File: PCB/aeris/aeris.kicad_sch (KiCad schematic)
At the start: 28 parts, among them J1 SHT45, J2 LPS22HB, J3 SCD40, J4 SGP41, J5 PMSA003A, Q1 BSS138, U1 74AHCT244, U3 ESP32-H2-SUPERMINI

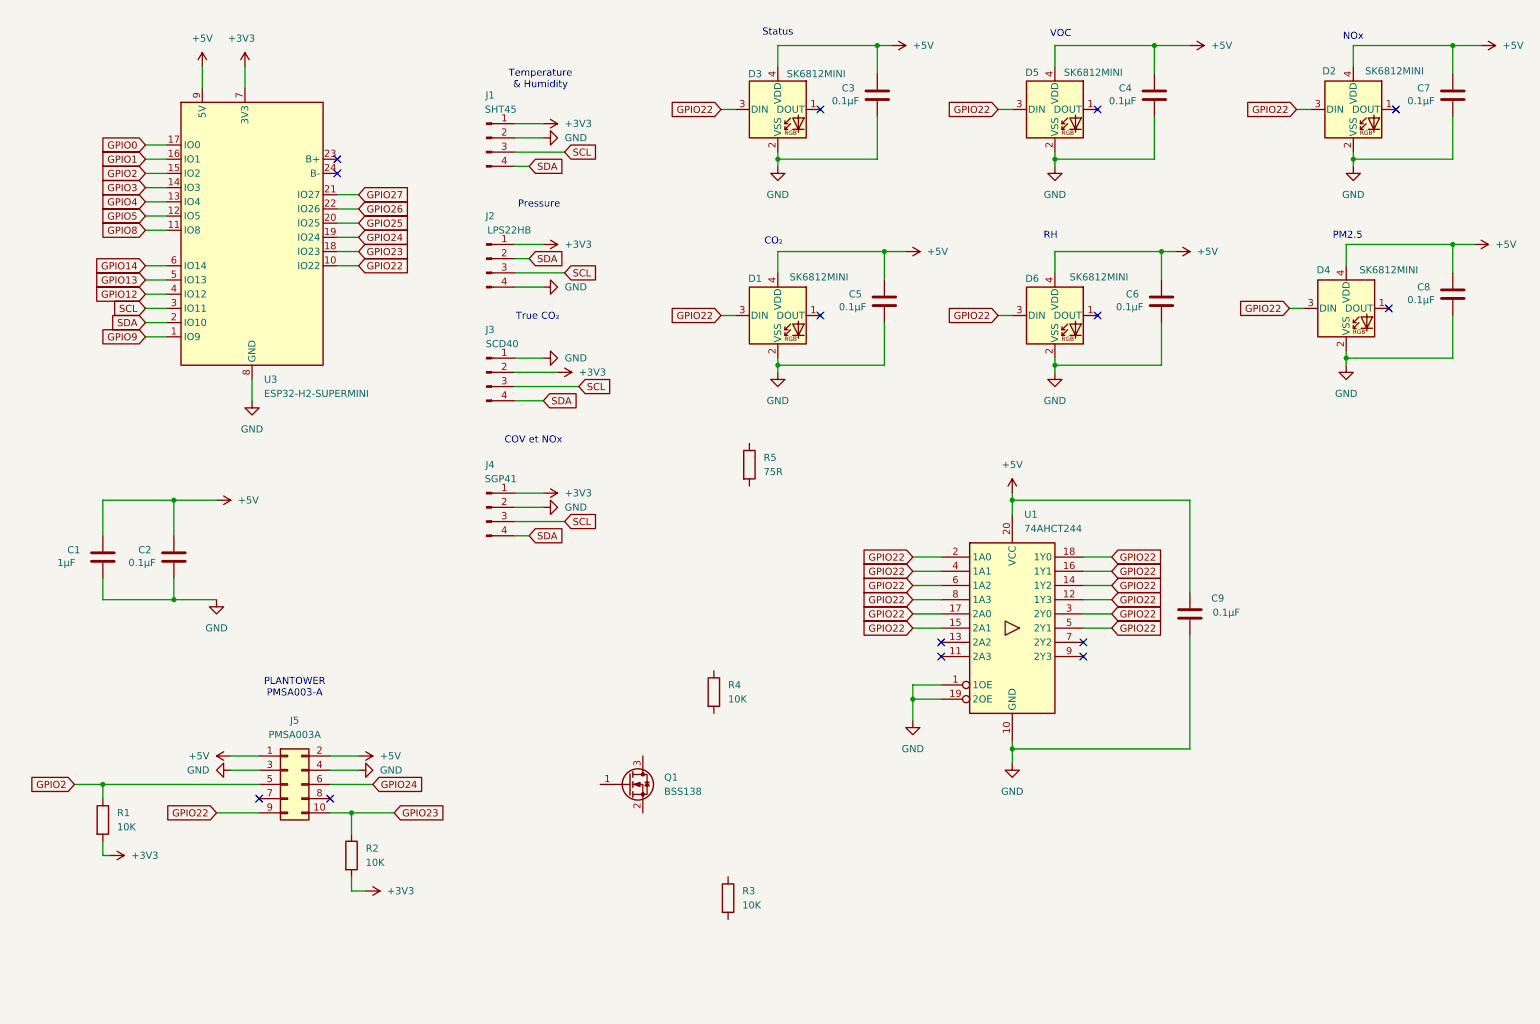
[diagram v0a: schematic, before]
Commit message: Add symbol library for ESP32-C6FH4-SuperMini to the project and update project GPIOs
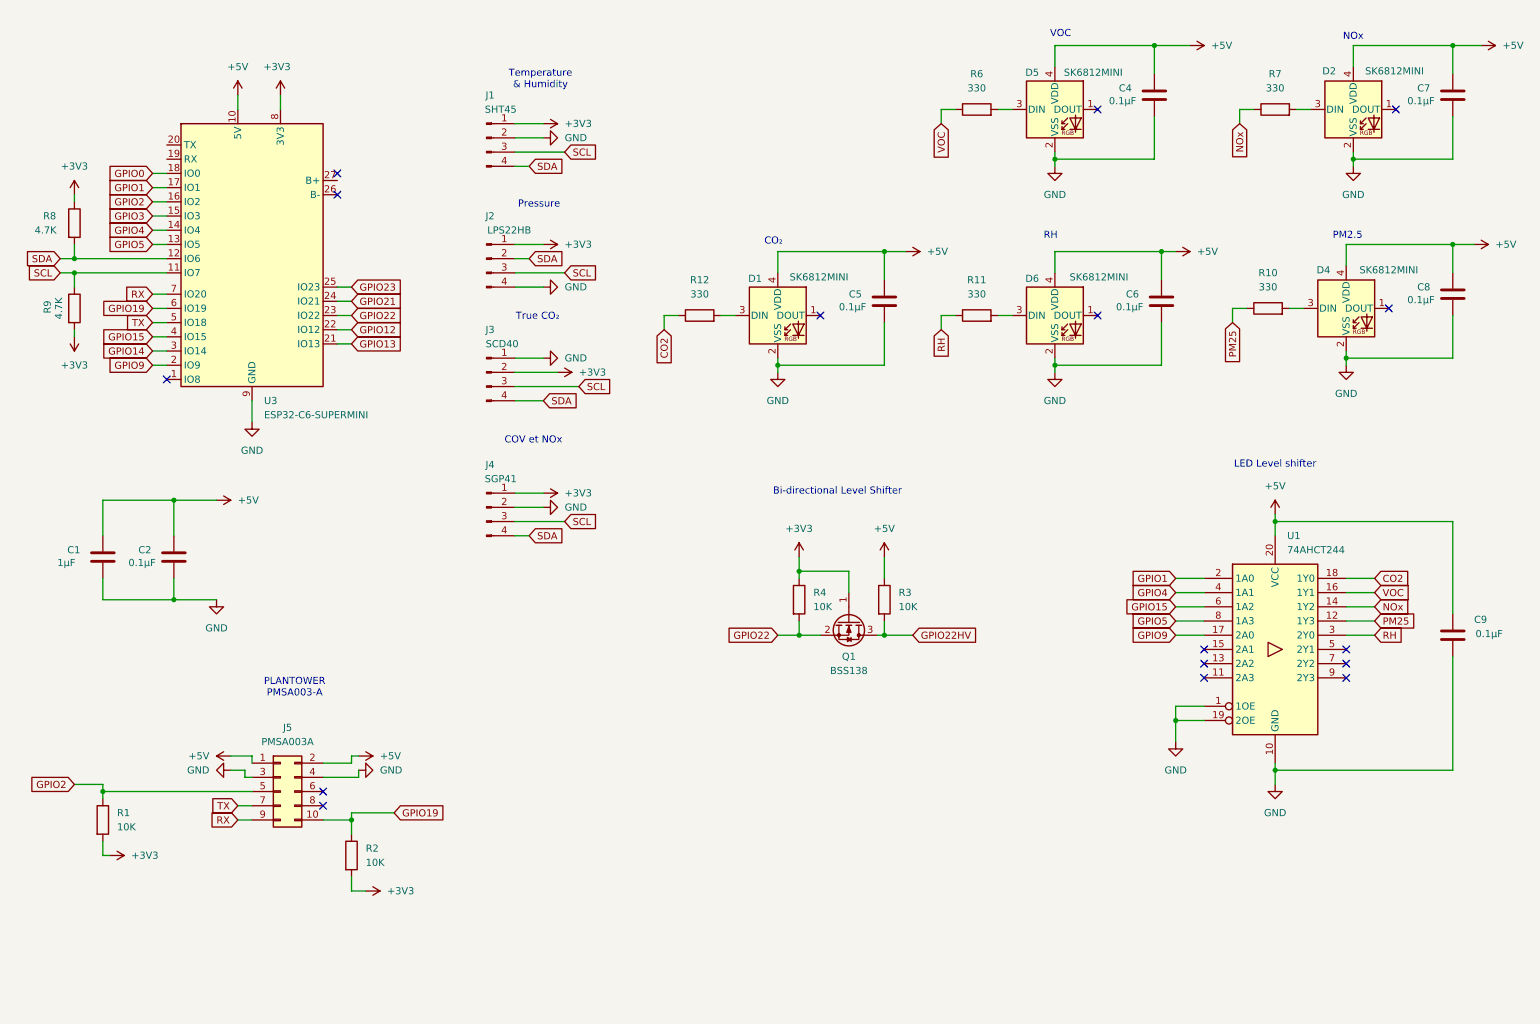
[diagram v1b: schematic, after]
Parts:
- removed C3: 0.1µF, Capacitor_SMD:C_1206_3216Metric, symbol Device:C
- removed D3: SK6812MINI, LED_SMD:LED_SK6812MINI_PLCC4_3.5x3.5mm_P1.75mm, symbol LED:SK6812MINI
- removed R5: 75R, symbol Device:R
- added R10, R11, R12, R6, R7: 330, symbol Device:R
- added R8, R9: 4.7K, Resistor_SMD:R_0805_2012Metric, symbol Device:R
- R1, R2, R3, R4: footprint (none) -> Resistor_SMD:R_0805_2012Metric
- U3: value ESP32-H2-SUPERMINI -> ESP32-C6-SUPERMINI; symbol ESP32H2-Supermini:ESP32-S3-MINI-1 -> ESP32-C6FH4-SuperMini:ESP32-C6FH4-SuperMini
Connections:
- net GPIO26 is gone; now on net GPIO12: U3.22 (IO12)
- net GPIO27 is gone; now on net GPIO13: U3.21 (IO13)
- net GPIO8 is gone; now on net SCL: U3.11 (IO7)
- net +3V3: now also Q1.1 (G), R4.1, U3.8 (3V3), R8.1, R9.2; no longer U3.7 (3V3)
- net +5V: now also R3.1, U3.10 (5V); no longer U3.9 (5V)
- net GND: now also U3.9 (GND); no longer U3.8 (GND)
- net GPIO0: now also U3.18 (IO0); no longer U3.17 (IO0)
- net GPIO1: now also U1.2 (1A0), U3.17 (IO1); no longer U3.16 (IO1)
- net GPIO12: no longer U3.4 (IO12)
- net GPIO13: no longer U3.5 (IO13)
- net GPIO14: now also U3.3 (IO14); no longer U3.6 (IO14)
- net GPIO2: now also U3.16 (IO2); no longer U3.15 (IO2)
- net GPIO22: now also Q1.2 (S), R4.2, U3.23 (IO22); no longer D1.3 (DIN), D2.3 (DIN), D4.3 (DIN), D5.3 (DIN), D6.3 (DIN), J5.9 (Pin_9), U1.12 (1Y3), U1.14 (1Y2), U1.15 (2A1), U1.16 (1Y1), U1.17 (2A0), U1.18 (1Y0), U1.2 (1A0), U1.3 (2Y0), U1.4 (1A1), U1.5 (2Y1), U1.6 (1A2), U1.8 (1A3), U3.10 (IO22)
- net GPIO23: now also U3.25 (IO23); no longer J5.10 (Pin_10), R2.1, U3.18 (IO23)
- net GPIO3: now also U3.15 (IO3); no longer U3.14 (IO3)
- net GPIO4: now also U1.4 (1A1), U3.14 (IO4); no longer U3.13 (IO4)
- net GPIO5: now also U1.8 (1A3), U3.13 (IO5); no longer U3.12 (IO5)
- net GPIO9: now also U1.17 (2A0), U3.2 (IO9); no longer U3.1 (IO9)
- net SCL: now also R9.1; no longer U3.3 (IO11)
- net SDA: now also U3.12 (IO6), R8.2; no longer U3.2 (IO10)
- net GPIO22HV: now reaches Q1.3 (D)
- net GPIO22HV: now also R3.2
- net GPIO21: now reaches U3.24 (IO21)
- net TX: now reaches J5.7 (Pin_7)
- net TX: now also U3.5 (IO18)
- net GPIO24: no longer names the net of U3.19 (RX)
- net GPIO24: no longer J5.6 (Pin_6)
- net GPIO25: no longer names the net of U3.20 (TX)
- new net: D4.3 (DIN), R10.2
- new net: D5.3 (DIN), R6.2
- new net: D2.3 (DIN), R7.2
- new net: D6.3 (DIN), R11.2
- new net: D1.3 (DIN), R12.2
- new net CO2: R12.1, U1.18 (1Y0)
- new net GPIO15: U1.6 (1A2), U3.4 (IO15)
- new net GPIO19: J5.10 (Pin_10), R2.1, U3.6 (IO19)
- new net NOx: R7.1, U1.14 (1Y2)
- new net PM25: R10.1, U1.12 (1Y3)
- new net RH: R11.1, U1.3 (2Y0)
- new net RX: J5.9 (Pin_9), U3.7 (IO20)
- new net VOC: R6.1, U1.16 (1Y1)
- no-connect marks 14 -> 16
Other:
- note added: "Bi-directional Level Shifter"
- note added: "LED Level shifter"
- note removed: "Status"
- moved on the sheet: C9, J5, Q1, R3, R4, U1

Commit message: PCB version 1.0 Update PIN assignment for better PCB routing
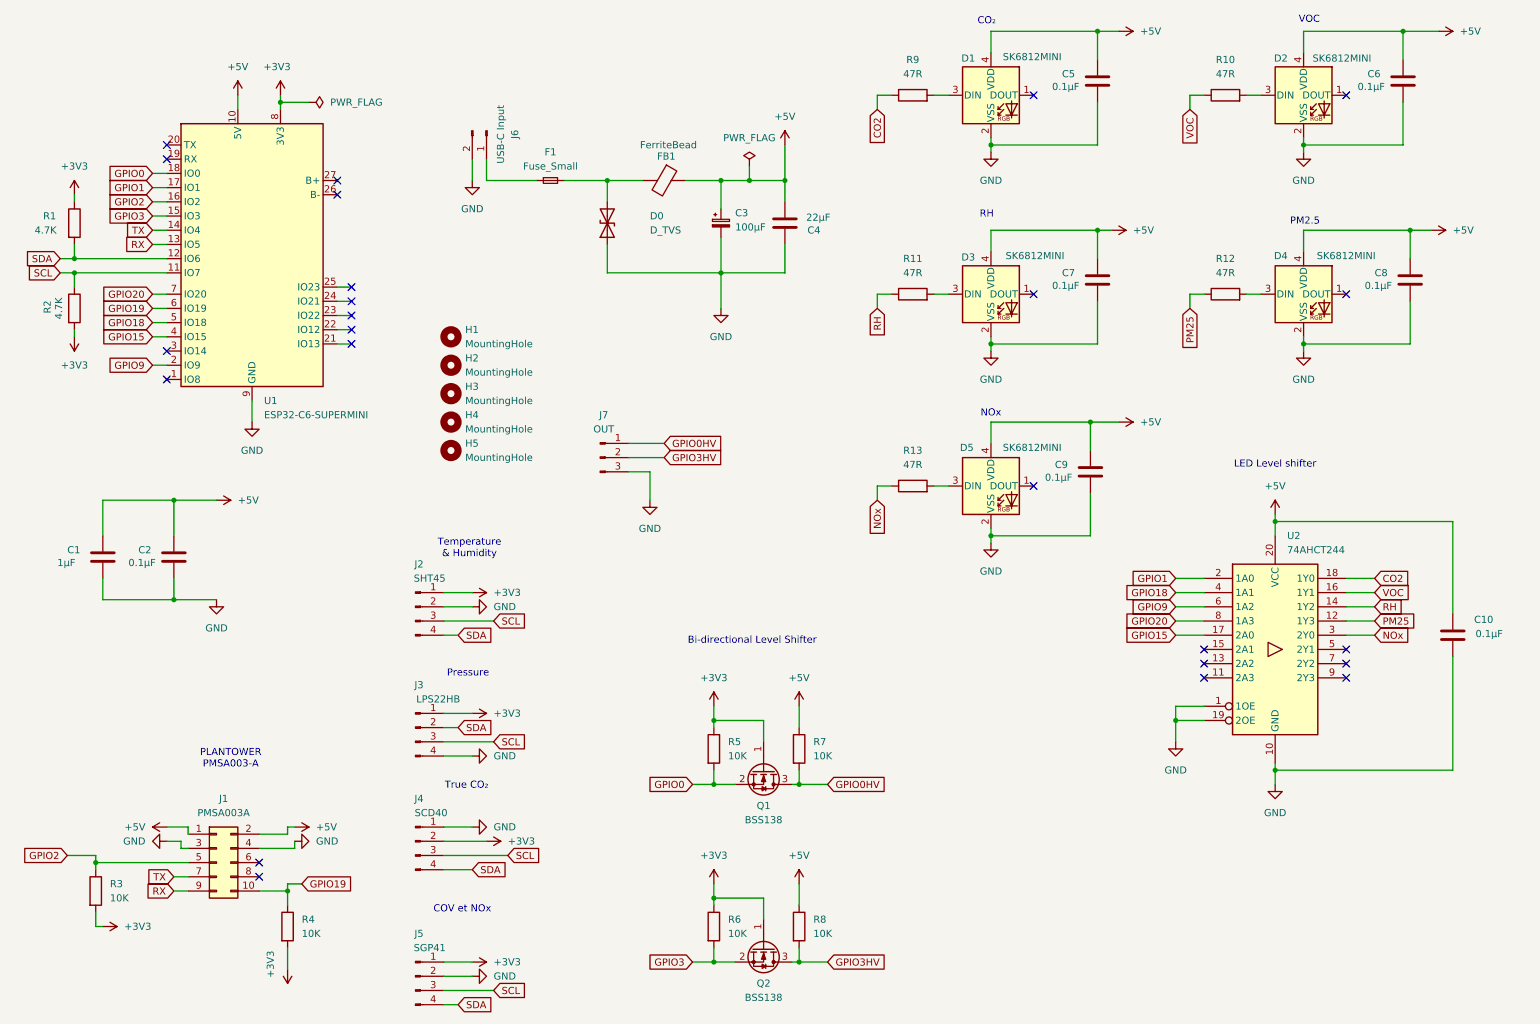
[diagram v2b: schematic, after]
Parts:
- added C3: 100µF, Capacitor_SMD:CP_Elec_6.3x5.9, symbol Device:C_Polarized_Small
- added C4: 22µF, Capacitor_SMD:C_0805_2012Metric, symbol Device:C
- added D0: D_TVS, Diode_SMD:D_SMB, symbol Device:D_TVS
- added F1: Fuse_Small, Fuse:Fuse_1206_3216Metric, symbol Device:Fuse_Small
- added FB1: FerriteBead, Inductor_SMD:L_1206_3216Metric, symbol Device:FerriteBead
- added H1, H2, H3, H4, H5: MountingHole, MountingHole:MountingHole_2.2mm_M2, symbol Mechanical:MountingHole
- added J6: USB-C Input, Connector_PinHeader_2.54mm:PinHeader_1x02_P2.54mm_Vertical, symbol Connector:Conn_01x02_Pin
- added J7: OUT, Connector_PinHeader_2.54mm:PinHeader_1x03_P2.54mm_Vertical, symbol Connector:Conn_01x03_Pin
- added Q2: BSS138, Package_TO_SOT_SMD:SOT-23, symbol Transistor_FET:BSS138
- added R6, R8: 10K, Resistor_SMD:R_0805_2012Metric, symbol Device:R
- C10: renamed from C9; footprint Capacitor_SMD:C_1206_3216Metric -> Capacitor_SMD:C_0805_2012Metric
- C2, C5, C8: footprint Capacitor_SMD:C_1206_3216Metric -> Capacitor_SMD:C_0805_2012Metric
- C6: renamed from C4; footprint Capacitor_SMD:C_1206_3216Metric -> Capacitor_SMD:C_0805_2012Metric
- C7: renamed from C6; footprint Capacitor_SMD:C_1206_3216Metric -> Capacitor_SMD:C_0805_2012Metric
- C9: renamed from C7; footprint Capacitor_SMD:C_1206_3216Metric -> Capacitor_SMD:C_0805_2012Metric
- J1: renamed from J5; footprint (none) -> esp32-h2-supermini:PLANTOWER_PMSA003-A
- J2: renamed from J1; footprint Connector_PinHeader_2.54mm:PinHeader_1x04_P2.54mm_Vertical -> esp32-h2-supermini:SHT45-Breakout
- J3: renamed from J2; footprint Connector_PinHeader_2.54mm:PinHeader_1x04_P2.54mm_Vertical -> esp32-h2-supermini:LPS22HB-Breakout
- J4: renamed from J3; footprint Connector_PinHeader_2.54mm:PinHeader_1x04_P2.54mm_Vertical -> esp32-h2-supermini:SCD40-Breakout
- J5: renamed from J4; footprint Connector_PinHeader_2.54mm:PinHeader_1x04_P2.54mm_Vertical -> esp32-h2-supermini:SGP41-Breakout
- R10: renamed from R6; value 330 -> 47R; footprint (none) -> Resistor_SMD:R_0805_2012Metric
- R11: value 330 -> 47R; footprint (none) -> Resistor_SMD:R_0805_2012Metric
- R12: renamed from R10; value 330 -> 47R; footprint (none) -> Resistor_SMD:R_0805_2012Metric
- R13: renamed from R7; value 330 -> 47R; footprint (none) -> Resistor_SMD:R_0805_2012Metric
- R9: renamed from R12; value 330 -> 47R; footprint (none) -> Resistor_SMD:R_0805_2012Metric
- U1: renamed from U3; footprint esp32-h2-supermini:ESP32H2-Supermini -> esp32-h2-supermini:ESP32C6-Supermini
- U2: renamed from U1; footprint (none) -> Package_SO:SOIC-20W_7.5x12.8mm_P1.27mm
- renumbered D5 to D2, D6 to D3, D2 to D5, R8 to R1, R9 to R2, R1 to R3, R2 to R4, R4 to R5, R3 to R7
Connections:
- net +3V3: now also Q2.1 (G), R6.1
- net +5V: now also C3.1, C4.2, FB1.1, R8.1
- net GND: now also C3.2, C4.1, D0.1 (A1), J6.2 (Pin_2), J7.3 (Pin_3)
- net GPIO0: now also Q1.2 (S), R5.2
- net GPIO15: now also U2.17 (2A0); no longer U2.6 (1A2)
- net GPIO3: now also Q2.2 (S), R6.2
- net GPIO9: now also U2.6 (1A2); no longer U2.17 (2A0)
- net NOx: now also U2.3 (2Y0); no longer U2.14 (1Y2)
- net RH: now also U2.14 (1Y2); no longer U2.3 (2Y0)
- net RX: now also U1.13 (IO5); no longer U1.7 (IO20)
- net TX: now also U1.14 (IO4); no longer U1.5 (IO18)
- net GPIO12: no longer names the net of U1.22 (IO12)
- net GPIO13: no longer names the net of U1.21 (IO13)
- net GPIO14: no longer names the net of U1.3 (IO14)
- net GPIO21: no longer names the net of U1.24 (IO21)
- removed net GPIO22: Q1.2 (S), R5.2, U1.23 (IO22)
- net GPIO22HV renamed GPIO0HV
- net GPIO0HV: now also J7.1 (Pin_1)
- net GPIO23: no longer names the net of U1.25 (IO23)
- net GPIO4 renamed GPIO18
- net GPIO18: now also U1.5 (IO18); no longer U1.14 (IO4)
- net GPIO5 renamed GPIO20
- net GPIO20: now also U1.7 (IO20); no longer U1.13 (IO5)
- new net: F1.1, J6.1 (Pin_1)
- new net: D0.2 (A2), F1.2, FB1.2
- new net GPIO3HV: J7.2 (Pin_2), Q2.3 (D), R8.2
- no-connect marks 16 -> 24
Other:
- moved on the sheet: C5, C6, C7, C8, C9, D1, D2, D3, D4, D5, J1, J2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
